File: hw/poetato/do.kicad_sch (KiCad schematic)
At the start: 9 parts, among them K1 AQY212GS, Q1 NTK3134N

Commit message: hw: sync symbols with kicadlib field text and value updates
Update Symbols from Library for kicadlib 8686346 (field text 1.27 mm) and
5b35b6c (units on misc R/C values). Value text sizes synced to the library
by script, since a Value reset would also reset power-symbol net names.
Restored BOM_Entry Manufacturer/Part Number and the R57 Power field that the
update cleared, and field positions it reset. Nudged R1, C6, Q6 and C75 text
clear of the larger power-symbol labels. ERC clean, netlist unchanged apart
from the intended values.
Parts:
- R52: value 10 -> 10Ω
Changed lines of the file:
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@@
 			(effects
 				(font
-					(size 0.9906 0.9906)
+					(size 1.27 1.27)
 				)
 				(justify left)
@@
 			(effects
 				(font
-					(size 1.016 1.016)
+					(size 1.27 1.27)
 				)
 				(justify left)
@@
 			(effects
 				(font
-					(size 0.9906 0.9906)
+					(size 1.27 1.27)
 				)
 				(justify left)
@@
 		(dnp no)
 		(fields_autoplaced yes)
-		(property "Reference" "#PWR088"
+		(property "Reference" "#PWR88"
 			(at 76.2 126.746 0)
 			(hide yes)
@@
 			(effects
 				(font
-					(size 0.508 0.508)
+					(size 1.27 1.27)
 				)
 			)
@@
 			(effects
 				(font
-					(size 0.762 0.762)
+					(size 1.27 1.27)
 				)
 			)
@@
 			(effects
 				(font
-					(size 1.524 1.524)
+					(size 1.27 1.27)
 				)
 			)
@@
 			(effects
 				(font
-					(size 1.524 1.524)
+					(size 1.27 1.27)
 				)
 			)
@@
 			(project "poetato"
 				(path "/f0f504bb-124c-46e5-ad39-032d3dfa78b3/7f50897c-81bd-4425-95ed-f5153c9db421/383af190-fccf-4fb0-8c6e-c0da9dc9d45c"
-					(reference "#PWR089")
+					(reference "#PWR89")
 					(unit 1)
 				)
 				(path "/f0f504bb-124c-46e5-ad39-032d3dfa78b3/7f50897c-81bd-4425-95ed-f5153c9db421/4d3cdf74-7a95-4e8d-9873-225f4679ebf7"
-					(reference "#PWR088")
+					(reference "#PWR88")
 					(unit 1)
 				)
@@
 			)
 		)
-		(property "Value" "10"
+		(property "Value" "10Ω"
 			(at 147.32 83.82 90)
 			(show_name no)
@@
 		(dnp no)
 		(fields_autoplaced yes)
-		(property "Reference" "#PWR090"
+		(property "Reference" "#PWR90"
 			(at 93.98 126.746 0)
 			(hide yes)
@@
 			(effects
 				(font
-					(size 0.508 0.508)
+					(size 1.27 1.27)
 				)
 			)
@@
 			(effects
 				(font
-					(size 0.762 0.762)
+					(size 1.27 1.27)
 				)
 			)
@@
 			(effects
 				(font
-					(size 1.524 1.524)
+					(size 1.27 1.27)
 				)
 			)
@@
 			(effects
 				(font
-					(size 1.524 1.524)
+					(size 1.27 1.27)
 				)
 			)
@@
 			(project "poetato"
 				(path "/f0f504bb-124c-46e5-ad39-032d3dfa78b3/7f50897c-81bd-4425-95ed-f5153c9db421/383af190-fccf-4fb0-8c6e-c0da9dc9d45c"
-					(reference "#PWR091")
+					(reference "#PWR91")
 					(unit 1)
 				)
 				(path "/f0f504bb-124c-46e5-ad39-032d3dfa78b3/7f50897c-81bd-4425-95ed-f5153c9db421/4d3cdf74-7a95-4e8d-9873-225f4679ebf7"
-					(reference "#PWR090")
+					(reference "#PWR90")
 					(unit 1)
 				)
@@
 			(effects
 				(font
-					(size 1.524 1.524)
+					(size 1.27 1.27)
 				)
 				(justify left)
@@
 			(effects
 				(font
-					(size 1.524 1.524)
+					(size 1.27 1.27)
 				)
 				(justify left)
@@
 		(dnp no)
 		(fields_autoplaced yes)
-		(property "Reference" "#PWR092"
+		(property "Reference" "#PWR92"
 			(at 106.68 63.754 0)
 			(hide yes)
@@
 			(effects
 				(font
-					(size 0.508 0.508)
+					(size 1.27 1.27)
 				)
 			)
@@
 			(effects
 				(font
-					(size 0.762 0.762)
+					(size 1.27 1.27)
 				)
 				(justify left)
@@
 			(effects
 				(font
-					(size 1.524 1.524)
+					(size 1.27 1.27)
 				)
 			)
@@
 			(effects
 				(font
-					(size 1.524 1.524)
+					(size 1.27 1.27)
 				)
 			)
@@
 			(project "poetato"
 				(path "/f0f504bb-124c-46e5-ad39-032d3dfa78b3/7f50897c-81bd-4425-95ed-f5153c9db421/383af190-fccf-4fb0-8c6e-c0da9dc9d45c"
-					(reference "#PWR093")
+					(reference "#PWR93")
 					(unit 1)
 				)
 				(path "/f0f504bb-124c-46e5-ad39-032d3dfa78b3/7f50897c-81bd-4425-95ed-f5153c9db421/4d3cdf74-7a95-4e8d-9873-225f4679ebf7"
-					(reference "#PWR092")
-					(unit 1)
-				)
+					(reference "#PWR92")
+					(unit 1)
+				)

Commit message: hw: fix local text collisions and add strap and BOM notes
- MCU: light-pipe note beside D14, TP64/TP65 references off the signal rows
- Ethernet: KSZ8081 strap summary (PHY address 1, RMII, auto-neg 100M),
  TP6 reference clear of POE_VDD
- IO: rating notes merged into the notes box
- DO: PhotoMOS note under K1
- Top level: frame and title around the BOM-only entries

Text and graphics only; ERC clean, netlist unchanged.
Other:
- note added: "PhotoMOS: 3 A, < 100 ms required"
- note removed: "PhotoMos: 3A, < 100ms req"
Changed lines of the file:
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@@
 		)
 	)
-	(text "PhotoMos: 3A, < 100ms req"
+	(text "PhotoMOS: 3 A, < 100 ms required"
 		(exclude_from_sim no)
-		(at 144.018 98.806 0)
+		(at 121.92 107.95 0)
 		(effects
 			(font

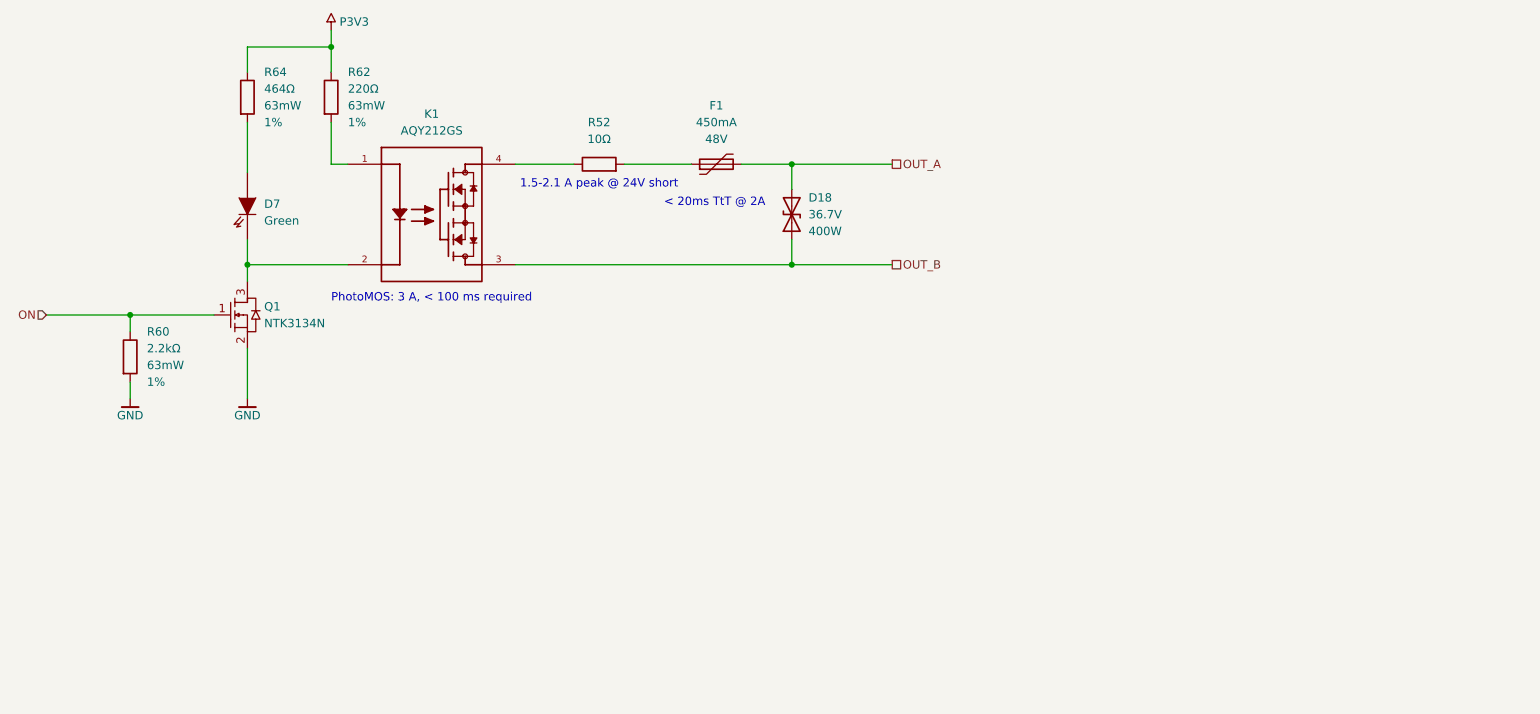
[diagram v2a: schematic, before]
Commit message: hw: schematic touch-ups, J3 updated from library
Layout touch-ups in KiCad. J3 (FTSH-105) pulled from kicadlib 81de170:
pin numbers without leading zeros (01-10 -> 1-10). Otherwise connectivity
and values unchanged; ERC clean. Project file picks up the Peripherals
sheet name.
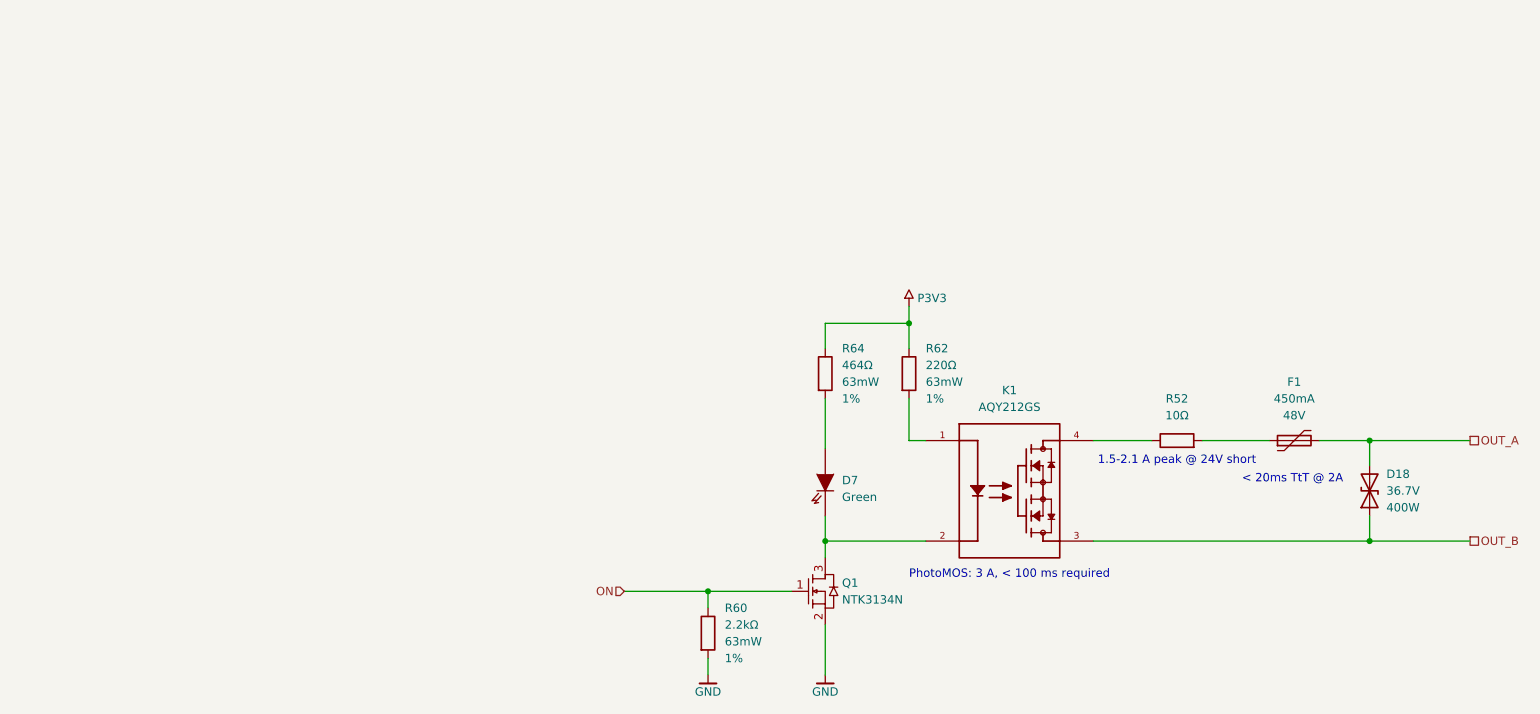
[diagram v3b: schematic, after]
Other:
- moved on the sheet: D18, D7, F1, K1, Q1, R52, R60, R62, R64
